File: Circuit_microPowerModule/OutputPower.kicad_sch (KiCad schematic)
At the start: 31 parts, among them U4 LM358, U7 MP2315S, U8 LM358

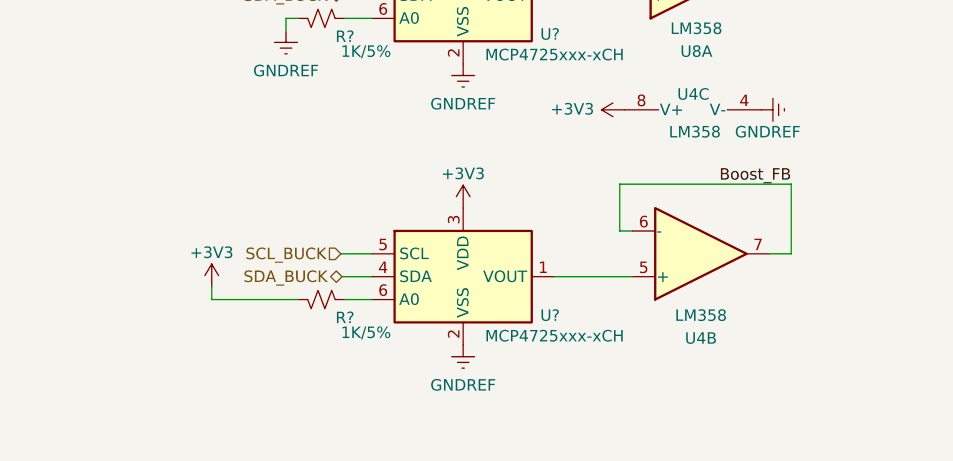
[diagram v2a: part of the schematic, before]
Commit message: added mikrobus header
added filter capacitance, I2C pull-up resistor
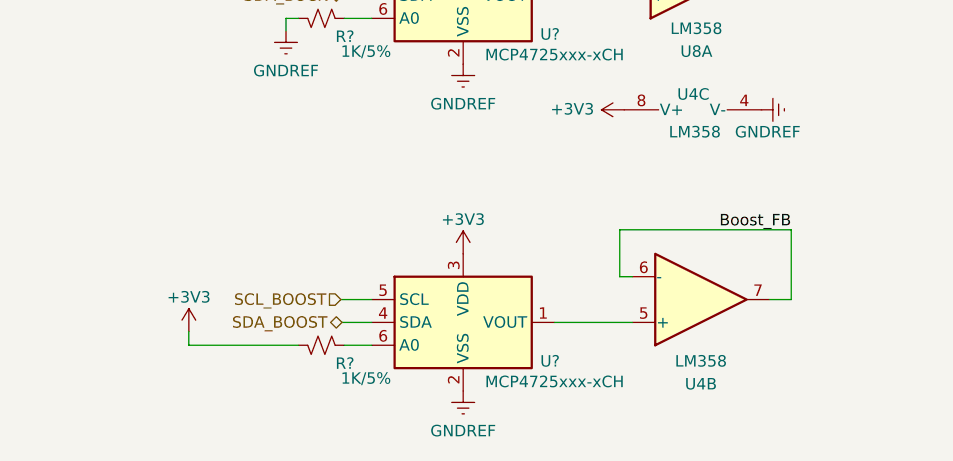
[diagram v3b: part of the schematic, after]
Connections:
- net SCL_BUCK: no longer U?.5 (SCL)
- net SDA_BUCK: no longer U?.4 (SDA)
- new net SCL_BOOST: U?.5 (SCL)
- new net SDA_BOOST: U?.4 (SDA)
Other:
- moved on the sheet: R?, U4B, U?
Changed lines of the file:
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@@
     (stroke (width 0) (type default))
   )
-  (wire (pts (xy 62.992 149.987) (xy 66.04 149.987))
+  (wire (pts (xy 62.992 155.067) (xy 66.04 155.067))
     (stroke (width 0) (type default))
   )
@@
     (stroke (width 0) (type default))
   )
-  (wire (pts (xy 62.738 147.447) (xy 66.04 147.447))
+  (wire (pts (xy 62.738 152.527) (xy 66.04 152.527))
     (stroke (width 0) (type default))
   )
@@
     (stroke (width 0) (type default))
   )
-  (wire (pts (xy 112.649 144.907) (xy 112.649 137.16))
+  (wire (pts (xy 112.649 149.987) (xy 112.649 142.24))
     (stroke (width 0) (type default))
   )
@@
     (stroke (width 0) (type default))
   )
-  (wire (pts (xy 48.26 148.59) (xy 48.26 149.987))
+  (wire (pts (xy 45.72 153.543) (xy 45.72 155.067))
     (stroke (width 0) (type default))
   )
@@
     (stroke (width 0) (type default))
   )
-  (wire (pts (xy 93.599 137.16) (xy 112.649 137.16))
+  (wire (pts (xy 93.599 142.24) (xy 112.649 142.24))
     (stroke (width 0) (type default))
   )
@@
     (stroke (width 0) (type default))
   )
-  (wire (pts (xy 93.599 137.16) (xy 93.599 142.367))
+  (wire (pts (xy 93.599 142.24) (xy 93.599 147.447))
     (stroke (width 0) (type default))
   )
@@
     (stroke (width 0) (type default))
   )
-  (wire (pts (xy 86.36 147.447) (xy 94.996 147.447))
+  (wire (pts (xy 86.36 152.527) (xy 94.996 152.527))
     (stroke (width 0) (type default))
   )
@@
     (stroke (width 0) (type default))
   )
-  (wire (pts (xy 62.611 144.907) (xy 66.04 144.907))
-    (stroke (width 0) (type default))
-  )
-  (wire (pts (xy 110.236 144.907) (xy 112.649 144.907))
-    (stroke (width 0) (type default))
-  )
-  (wire (pts (xy 93.599 142.367) (xy 94.996 142.367))
+  (wire (pts (xy 62.611 149.987) (xy 66.04 149.987))
+    (stroke (width 0) (type default))
+  )
+  (wire (pts (xy 110.236 149.987) (xy 112.649 149.987))
+    (stroke (width 0) (type default))
+  )
+  (wire (pts (xy 93.599 147.447) (xy 94.996 147.447))
     (stroke (width 0) (type default))
   )
@@
     (stroke (width 0) (type default))
   )
-  (wire (pts (xy 48.26 149.987) (xy 57.912 149.987))
+  (wire (pts (xy 45.72 155.067) (xy 57.912 155.067))
     (stroke (width 0) (type default))
   )
@@
     (effects (font (size 1.27 1.27)) (justify right bottom))
   )
-  (label "Boost_FB" (at 112.649 137.16 180) (fields_autoplaced)
+  (label "Boost_FB" (at 112.649 142.24 180) (fields_autoplaced)
     (effects (font (size 1.27 1.27)) (justify right bottom))
   )
@@
     (effects (font (size 1.27 1.27)) (justify left))
   )
-  (hierarchical_label "SCL_BUCK" (shape input) (at 62.611 144.907 180) (fields_autoplaced)
+  (hierarchical_label "SCL_BOOST" (shape input) (at 62.611 149.987 180) (fields_autoplaced)
     (effects (font (size 1.27 1.27)) (justify right))
   )
-  (hierarchical_label "SDA_BUCK" (shape bidirectional) (at 62.738 147.447 180) (fields_autoplaced)
+  (hierarchical_label "SDA_BOOST" (shape bidirectional) (at 62.738 152.527 180) (fields_autoplaced)
     (effects (font (size 1.27 1.27)) (justify right))
   )
@@
     )
   )
-  (symbol (lib_id "Device:R_Small_US") (at 60.452 149.987 270) (mirror x) (unit 1)
-    (in_bom yes) (on_board yes) (dnp no)
-    (property "Reference" "R?" (at 64.135 152.019 90)
+  (symbol (lib_id "Device:R_Small_US") (at 60.452 155.067 270) (mirror x) (unit 1)
+    (in_bom yes) (on_board yes) (dnp no)
+    (property "Reference" "R?" (at 64.135 157.099 90)
       (effects (font (size 1.27 1.27)) (justify right))
     )
-    (property "Value" "1K/5%" (at 68.199 153.67 90)
+    (property "Value" "1K/5%" (at 68.199 158.75 90)
       (effects (font (size 1.27 1.27)) (justify right))
     )
-    (property "Footprint" "Resistor_SMD:R_0603_1608Metric" (at 60.452 149.987 0)
-      (effects (font (size 1.27 1.27)) hide)
-    )
-    (property "Datasheet" "~" (at 60.452 149.987 0)
+    (property "Footprint" "Resistor_SMD:R_0603_1608Metric" (at 60.452 155.067 0)
+      (effects (font (size 1.27 1.27)) hide)
+    )
+    (property "Datasheet" "~" (at 60.452 155.067 0)
       (effects (font (size 1.27 1.27)) hide)
     )
@@
     )
   )
-  (symbol (lib_id "Analog_DAC:MCP4725xxx-xCH") (at 76.2 147.447 0) (unit 1)
-    (in_bom yes) (on_board yes) (dnp no)
-    (property "Reference" "U?" (at 85.852 151.765 0)
-      (effects (font (size 1.27 1.27)))
-    )
-    (property "Value" "MCP4725xxx-xCH" (at 86.36 154.051 0)
-      (effects (font (size 1.27 1.27)))
-    )
-    (property "Footprint" "Package_TO_SOT_SMD:SOT-23-6" (at 76.2 153.797 0)
-      (effects (font (size 1.27 1.27)) hide)
-    )
-    (property "Datasheet" "http://ww1.microchip.com/downloads/en/DeviceDoc/22039d.pdf" (at 76.2 147.447 0)
+  (symbol (lib_id "Analog_DAC:MCP4725xxx-xCH") (at 76.2 152.527 0) (unit 1)
+    (in_bom yes) (on_board yes) (dnp no)
+    (property "Reference" "U?" (at 85.852 156.845 0)
+      (effects (font (size 1.27 1.27)))
+    )
+    (property "Value" "MCP4725xxx-xCH" (at 86.36 159.131 0)
+      (effects (font (size 1.27 1.27)))
+    )
+    (property "Footprint" "Package_TO_SOT_SMD:SOT-23-6" (at 76.2 158.877 0)
+      (effects (font (size 1.27 1.27)) hide)
+    )
+    (property "Datasheet" "http://ww1.microchip.com/downloads/en/DeviceDoc/22039d.pdf" (at 76.2 152.527 0)
       (effects (font (size 1.27 1.27)) hide)
     )
@@
     )
   )
-  (symbol (lib_id "power:+3V3") (at 48.26 148.59 0) (unit 1)
-    (in_bom yes) (on_board yes) (dnp no) (fields_autoplaced)
-    (property "Reference" "#PWR031" (at 48.26 152.4 0)
-      (effects (font (size 1.27 1.27)) hide)
-    )
-    (property "Value" "+3V3" (at 48.26 144.78 0)
-      (effects (font (size 1.27 1.27)))
-    )
-    (property "Footprint" "" (at 48.26 148.59 0)
-      (effects (font (size 1.27 1.27)) hide)
-    )
-    (property "Datasheet" "" (at 48.26 148.59 0)
+  (symbol (lib_id "power:+3V3") (at 45.72 153.543 0) (unit 1)
+    (in_bom yes) (on_board yes) (dnp no) (fields_autoplaced)
+    (property "Reference" "#PWR031" (at 45.72 157.353 0)
+      (effects (font (size 1.27 1.27)) hide)
+    )
+    (property "Value" "+3V3" (at 45.72 149.733 0)
+      (effects (font (size 1.27 1.27)))
+    )
+    (property "Footprint" "" (at 45.72 153.543 0)
+      (effects (font (size 1.27 1.27)) hide)
+    )
+    (property "Datasheet" "" (at 45.72 153.543 0)
       (effects (font (size 1.27 1.27)) hide)
     )
@@
     )
   )
-  (symbol (lib_id "power:+3V3") (at 76.2 139.827 0) (unit 1)
-    (in_bom yes) (on_board yes) (dnp no) (fields_autoplaced)
-    (property "Reference" "#PWR033" (at 76.2 143.637 0)
-      (effects (font (size 1.27 1.27)) hide)
-    )
-    (property "Value" "+3V3" (at 76.2 136.017 0)
-      (effects (font (size 1.27 1.27)))
-    )
-    (property "Footprint" "" (at 76.2 139.827 0)
-      (effects (font (size 1.27 1.27)) hide)
-    )
-    (property "Datasheet" "" (at 76.2 139.827 0)
+  (symbol (lib_id "power:+3V3") (at 76.2 144.907 0) (unit 1)
+    (in_bom yes) (on_board yes) (dnp no) (fields_autoplaced)
+    (property "Reference" "#PWR033" (at 76.2 148.717 0)
+      (effects (font (size 1.27 1.27)) hide)
+    )
+    (property "Value" "+3V3" (at 76.2 141.097 0)
+      (effects (font (size 1.27 1.27)))
+    )
+    (property "Footprint" "" (at 76.2 144.907 0)
+      (effects (font (size 1.27 1.27)) hide)
+    )
+    (property "Datasheet" "" (at 76.2 144.907 0)
       (effects (font (size 1.27 1.27)) hide)
     )
@@
     )
   )
-  (symbol (lib_id "power:GNDREF") (at 76.2 155.067 0) (unit 1)
-    (in_bom yes) (on_board yes) (dnp no) (fields_autoplaced)
-    (property "Reference" "#PWR032" (at 76.2 161.417 0)
-      (effects (font (size 1.27 1.27)) hide)
-    )
-    (property "Value" "GNDREF" (at 76.2 159.512 0)
-      (effects (font (size 1.27 1.27)))
-    )
-    (property "Footprint" "" (at 76.2 155.067 0)
-      (effects (font (size 1.27 1.27)) hide)
-    )
-    (property "Datasheet" "" (at 76.2 155.067 0)
+  (symbol (lib_id "power:GNDREF") (at 76.2 160.147 0) (unit 1)
+    (in_bom yes) (on_board yes) (dnp no) (fields_autoplaced)
+    (property "Reference" "#PWR032" (at 76.2 166.497 0)
+      (effects (font (size 1.27 1.27)) hide)
+    )
+    (property "Value" "GNDREF" (at 76.2 164.592 0)
+      (effects (font (size 1.27 1.27)))
+    )
+    (property "Footprint" "" (at 76.2 160.147 0)
+      (effects (font (size 1.27 1.27)) hide)
+    )
+    (property "Datasheet" "" (at 76.2 160.147 0)
       (effects (font (size 1.27 1.27)) hide)
     )
@@
     )
   )
-  (symbol (lib_id "Amplifier_Operational:LM358") (at 102.616 144.907 0) (mirror x) (unit 2)
-    (in_bom yes) (on_board yes) (dnp no)
-    (property "Reference" "U4" (at 102.616 154.305 0)
-      (effects (font (size 1.27 1.27)))
-    )
-    (property "Value" "LM358" (at 102.616 151.765 0)
-      (effects (font (size 1.27 1.27)))
-    )
-    (property "Footprint" "" (at 102.616 144.907 0)
-      (effects (font (size 1.27 1.27)) hide)
-    )
-    (property "Datasheet" "http://www.ti.com/lit/ds/symlink/lm2904-n.pdf" (at 102.616 144.907 0)
-      (effects (font (size 1.27 1.27)) hide)
-    )
+  (symbol (lib_id "Amplifier_Operational:LM358") (at 102.616 149.987 0) (mirror x) (unit 2)
+    (in_bom yes) (on_board yes) (dnp no)
+    (property "Reference" "U4" (at 102.616 159.385 0)
+      (effects (font (size 1.27 1.27)))
+    )
+    (property "Value" "LM358" (at 102.616 156.845 0)
+      (effects (font (size 1.27 1.27)))
+    )
+    (property "Footprint" "" (at 102.616 149.987 0)
+      (effects (font (size 1.27 1.27)) hide)
+    )
+    (property "Datasheet" "http://www.ti.com/lit/ds/symlink/lm2904-n.pdf" (at 102.616 149.987 0)
+      (effects (font (size 1.27 1.27)) hide)
+    )

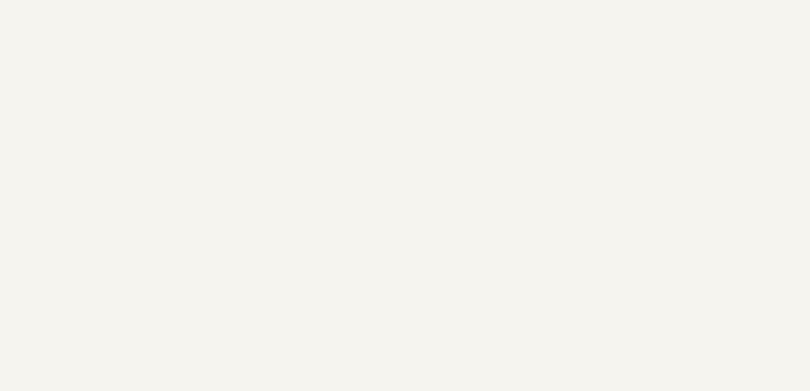
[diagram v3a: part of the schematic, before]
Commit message: added schematic svg file
added encoder wire, mikrobus connect
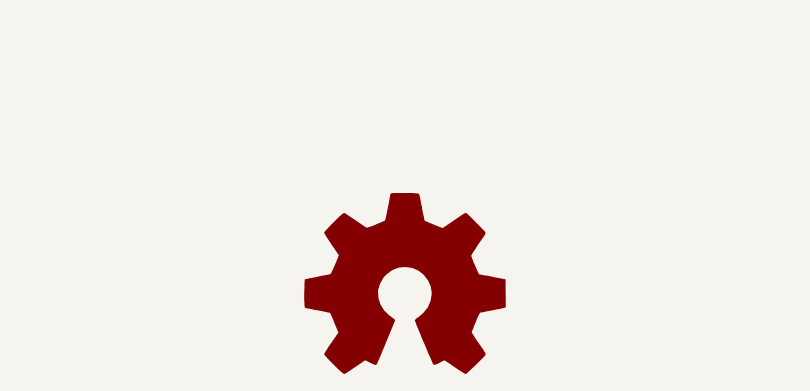
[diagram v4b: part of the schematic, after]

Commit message: change licenses
updated some footprint, create nokia 5110 lcd module pcb symbol, updated reademe
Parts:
- D5: footprint (none) -> Diode_SMD:D_SMC
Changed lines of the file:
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@@
       (effects (font (size 1.27 1.27)))
     )
-    (property "Footprint" "" (at 96.393 34.036 90)
+    (property "Footprint" "Diode_SMD:D_SMC" (at 96.393 34.036 90)
       (effects (font (size 1.27 1.27)) hide)
     )

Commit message: update components footprint
check boost VR component, added Nokia 5110 LCD 3D module
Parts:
- C2, C3, C6: footprint (none) -> Capacitor_SMD:C_0603_1608Metric
- L1, L2: footprint (none) -> Inductor_SMD_Wurth:L_Wurth_WE-LQSH-2512
- U4, U8: footprint (none) -> Package_TO_SOT_SMD:TSOT-23-8
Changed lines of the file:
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@@
       (effects (font (size 1.27 1.27)) (justify left))
     )
-    (property "Footprint" "" (at 113.411 70.104 0)
+    (property "Footprint" "Capacitor_SMD:C_0603_1608Metric" (at 113.411 70.104 0)
       (effects (font (size 1.27 1.27)) hide)
     )
@@
       (effects (font (size 1.27 1.27)) (justify left))
     )
-    (property "Footprint" "" (at 56.515 80.518 0)
+    (property "Footprint" "Capacitor_SMD:C_0603_1608Metric" (at 56.515 80.518 0)
       (effects (font (size 1.27 1.27)) hide)
     )
@@
       (effects (font (size 1.27 1.27)))
     )
-    (property "Footprint" "" (at 81.28 25.4 0)
+    (property "Footprint" "Inductor_SMD_Wurth:L_Wurth_WE-LQSH-2512" (at 81.28 25.4 0)
       (effects (font (size 1.27 1.27)) hide)
     )
@@
       (effects (font (size 1.27 1.27)))
     )
-    (property "Footprint" "" (at 121.412 72.771 0)
+    (property "Footprint" "Inductor_SMD_Wurth:L_Wurth_WE-LQSH-2512" (at 121.412 72.771 0)
       (effects (font (size 1.27 1.27)) hide)
     )
@@
       (effects (font (size 1.27 1.27)))
     )
-    (property "Footprint" "" (at 102.108 113.665 0)
+    (property "Footprint" "Package_TO_SOT_SMD:TSOT-23-8" (at 102.108 113.665 0)
       (effects (font (size 1.27 1.27)) hide)
     )
@@
       (effects (font (size 1.27 1.27)) (justify left))
     )
-    (property "Footprint" "" (at 101.727 126.365 0)
+    (property "Footprint" "Package_TO_SOT_SMD:TSOT-23-8" (at 101.727 126.365 0)
       (effects (font (size 1.27 1.27)) hide)
     )
@@
       (effects (font (size 1.27 1.27)))
     )
-    (property "Footprint" "" (at 102.616 149.987 0)
+    (property "Footprint" "Package_TO_SOT_SMD:TSOT-23-8" (at 102.616 149.987 0)
       (effects (font (size 1.27 1.27)) hide)
     )
@@
       (effects (font (size 1.27 1.27)) (justify left))
     )
-    (property "Footprint" "" (at 122.301 85.979 0)
-      (effects (font (size 1.27 1.27)) hide)
-    )
+    (property "Footprint" "Capacitor_SMD:C_0603_1608Metric" (at 122.301 85.979 0)
+      (effects (font (size 1.27 1.27)) hide)
+    )
